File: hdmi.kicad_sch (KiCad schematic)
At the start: 44 parts, among them J13 46756-1001, Q22 NX138BKMYL, U43 NTS0102GT, U44 TPD4E02B04DQA, U45 TPD4E02B04DQA, U46 TPD4E02B04DQA

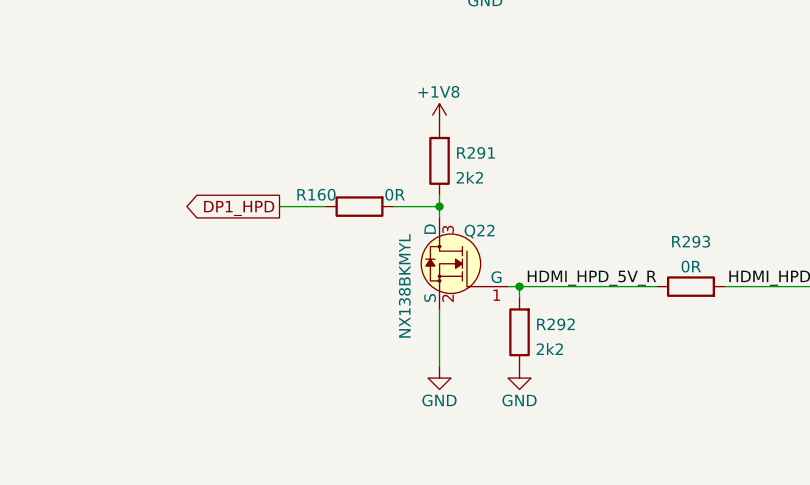
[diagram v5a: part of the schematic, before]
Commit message: Replaced NX138BKMYL with PJE138K transistor [#40527]
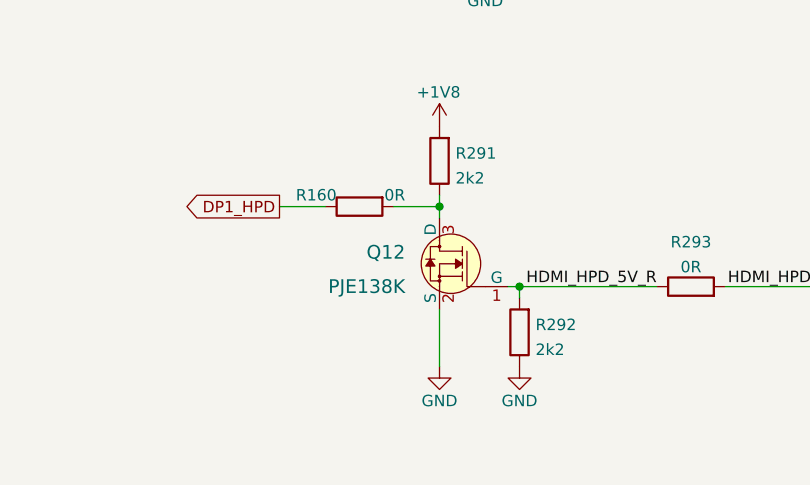
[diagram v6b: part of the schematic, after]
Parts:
- removed Q22: NX138BKMYL, jetson-orin-baseboard-footprints:DFN1006-3, symbol jetson-orin-baseboard:NX138BKMYL
- added Q12: PJE138K, antmicro-footprints:SOT-523, symbol antmicroTransistorsFETsMOSFETsSingle:PJE138K
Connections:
- net GND: now also Q12.2 (S)
- net HDMI_HPD_5V_R: now also Q12.1 (G)
- net at R160.2, R291.1: now also Q12.3 (D)
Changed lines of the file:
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@@
     (pin "2")
+  )
+  (symbol (lib_id "antmicroTransistorsFETsMOSFETsSingle:PJE138K") (at 250.19 182.88 0) (mirror y) (unit 1)
+    (in_bom yes) (on_board yes) (fields_autoplaced)
+    (property "Reference" "Q12" (id 0) (at 246.38 181.61 0)
+      (effects (font (size 1.524 1.524)) (justify left))
+    )
+    (property "Value" "PJE138K" (id 1) (at 246.38 185.42 0)
+      (effects (font (size 1.524 1.524)) (justify left))
+    )
+    (property "Footprint" "antmicro-footprints:SOT-523" (id 2) (at 245.11 177.8 0)
+      (effects (font (size 1.524 1.524)) (justify left) hide)
+    )
+    (property "Datasheet" "https://www.mouser.pl/datasheet/2/1057/PJE138K-1876698.pdf" (id 3) (at 245.11 175.26 0)
+      (effects (font (size 1.524 1.524)) (justify left) hide)
+    )
+    (property "MPN" "PJE138K_R1_00001" (id 4) (at 233.68 172.72 0)
+      (effects (font (size 1.524 1.524)) (justify left) hide)
+    )
+    (property "Manufacturer" "Panjit" (id 5) (at 245.11 172.72 0)
+      (effects (font (size 1.524 1.524)) (justify left) hide)
+    )
+    (pin "1")
+    (pin "2")
+    (pin "3")
   )
   (symbol (lib_id "jetson-orin-baseboard:C_100n_0402") (at 129.54 195.58 270) (mirror x) (unit 1)
@@
     (pin "2")
   )
-  (symbol (lib_id "jetson-orin-baseboard:NX138BKMYL") (at 250.19 182.88 0) (mirror y) (unit 1)
-    (in_bom yes) (on_board yes)
-    (property "Reference" "Q22" (id 0) (at 252.8824 179.2478 0)
-      (effects (font (size 1.27 1.27)) (justify right))
-    )
-    (property "Value" "NX138BKMYL" (id 1) (at 246.38 185.42 90))
-    (property "Footprint" "jetson-orin-baseboard-footprints:DFN1006-3" (id 2) (at 245.11 177.8 0)
-      (effects (font (size 1.524 1.524)) (justify left) hide)
-    )
-    (property "Datasheet" "https://www.mouser.pl/datasheet/2/916/NX138BKM-1919503.pdf" (id 3) (at 245.11 175.26 0)
-      (effects (font (size 1.524 1.524)) (justify left) hide)
-    )
-    (property "MPN" "NX138BKMYL" (id 4) (at 245.11 170.18 0)
-      (effects (font (size 1.524 1.524)) (justify left) hide)
-    )
-    (property "Manufacturer" "Nexperia" (id 5) (at 245.11 154.94 0)
-      (effects (font (size 1.524 1.524)) (justify left) hide)
-    )
-    (pin "1")
-    (pin "2")
-    (pin "3")
-  )
   (symbol (lib_id "jetson-orin-baseboard:C_100n_0402") (at 129.54 99.06 270) (mirror x) (unit 1)

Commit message: Replaced PCA9547 with PI4MSD5V9548AZDEX to support 1.8V I2C voltages for cameras [#40392]
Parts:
- R34, R35: footprint jetson-orin-baseboard-footprints:EXB18V -> antmicro-footprints:EXB18V; symbol jetson-orin-baseboard:4x0R_0201_array -> antmicroResistorNetworksArrays:4x0R_0201_array
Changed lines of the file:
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@@
     (pin "2")
   )
-  (symbol (lib_id "jetson-orin-baseboard:4x0R_0201_array") (at 200.66 85.09 180) (unit 1)
+  (symbol (lib_id "antmicroResistorNetworksArrays:4x0R_0201_array") (at 200.66 85.09 180) (unit 1)
     (in_bom yes) (on_board yes) (fields_autoplaced)
     (property "Reference" "R34" (id 0) (at 201.295 82.55 0))
@@
       (effects (font (size 1.524 1.524)) hide)
     )
-    (property "Footprint" "jetson-orin-baseboard-footprints:EXB18V" (id 2) (at 205.74 104.14 0)
+    (property "Footprint" "antmicro-footprints:EXB18V" (id 2) (at 205.74 104.14 0)
       (effects (font (size 1.524 1.524)) (justify left) hide)
     )
@@
     (pin "1")
   )
-  (symbol (lib_id "jetson-orin-baseboard:4x0R_0201_array") (at 201.93 115.57 0) (mirror y) (unit 1)
+  (symbol (lib_id "antmicroResistorNetworksArrays:4x0R_0201_array") (at 201.93 115.57 0) (mirror y) (unit 1)
     (in_bom yes) (on_board yes) (fields_autoplaced)
     (property "Reference" "R35" (id 0) (at 202.565 100.5672 0))
@@
       (effects (font (size 1.524 1.524)) hide)
     )
-    (property "Footprint" "jetson-orin-baseboard-footprints:EXB18V" (id 2) (at 207.01 96.52 0)
-      (effects (font (size 1.524 1.524)) (justify left) hide)
-    )
+    (property "Footprint" "antmicro-footprints:EXB18V" (id 2) (at 207.01 96.52 0)
+      (effects (font (size 1.524 1.524)) (justify left) hide)
+    )

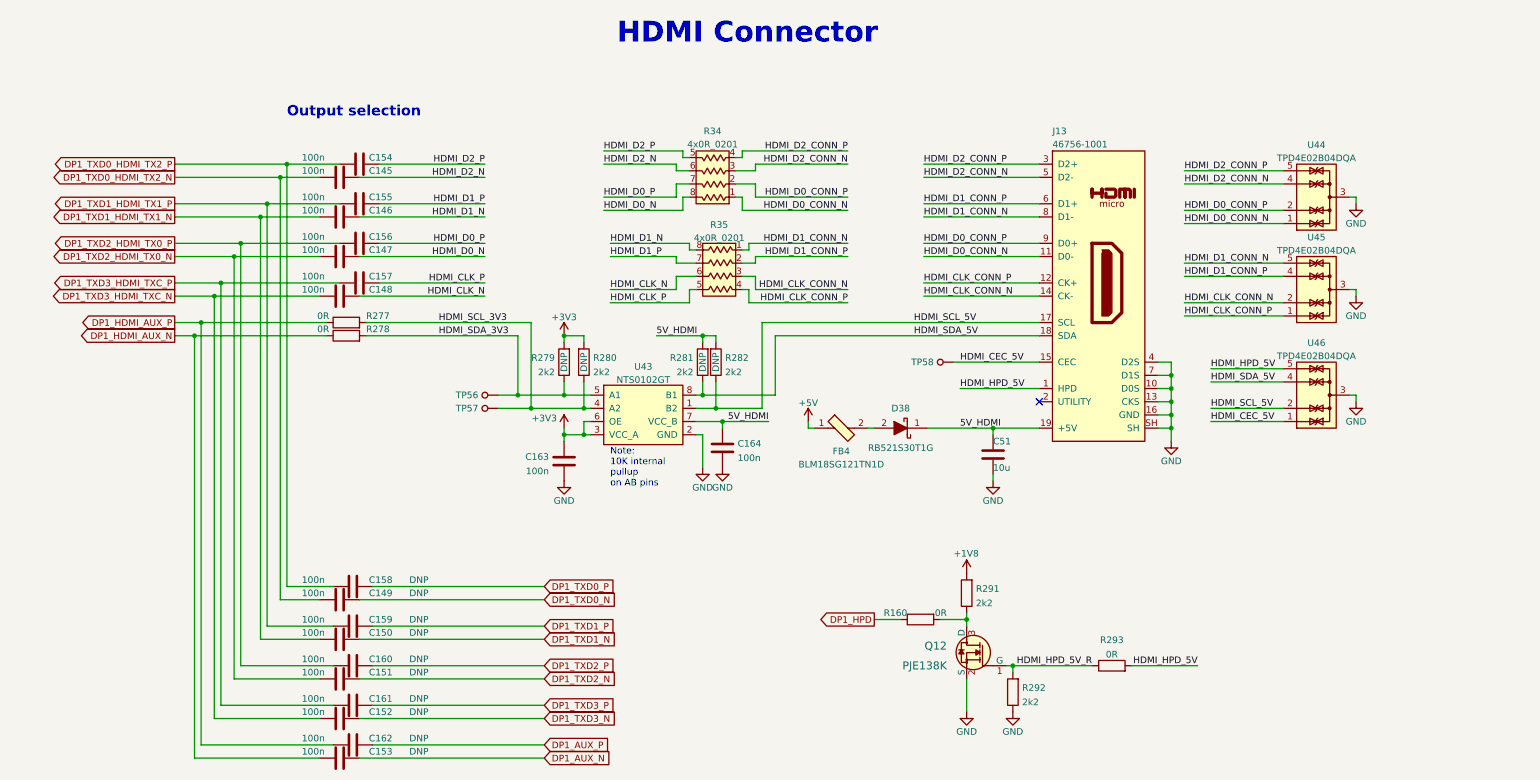
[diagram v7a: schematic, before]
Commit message: BOM reduction [#40581]
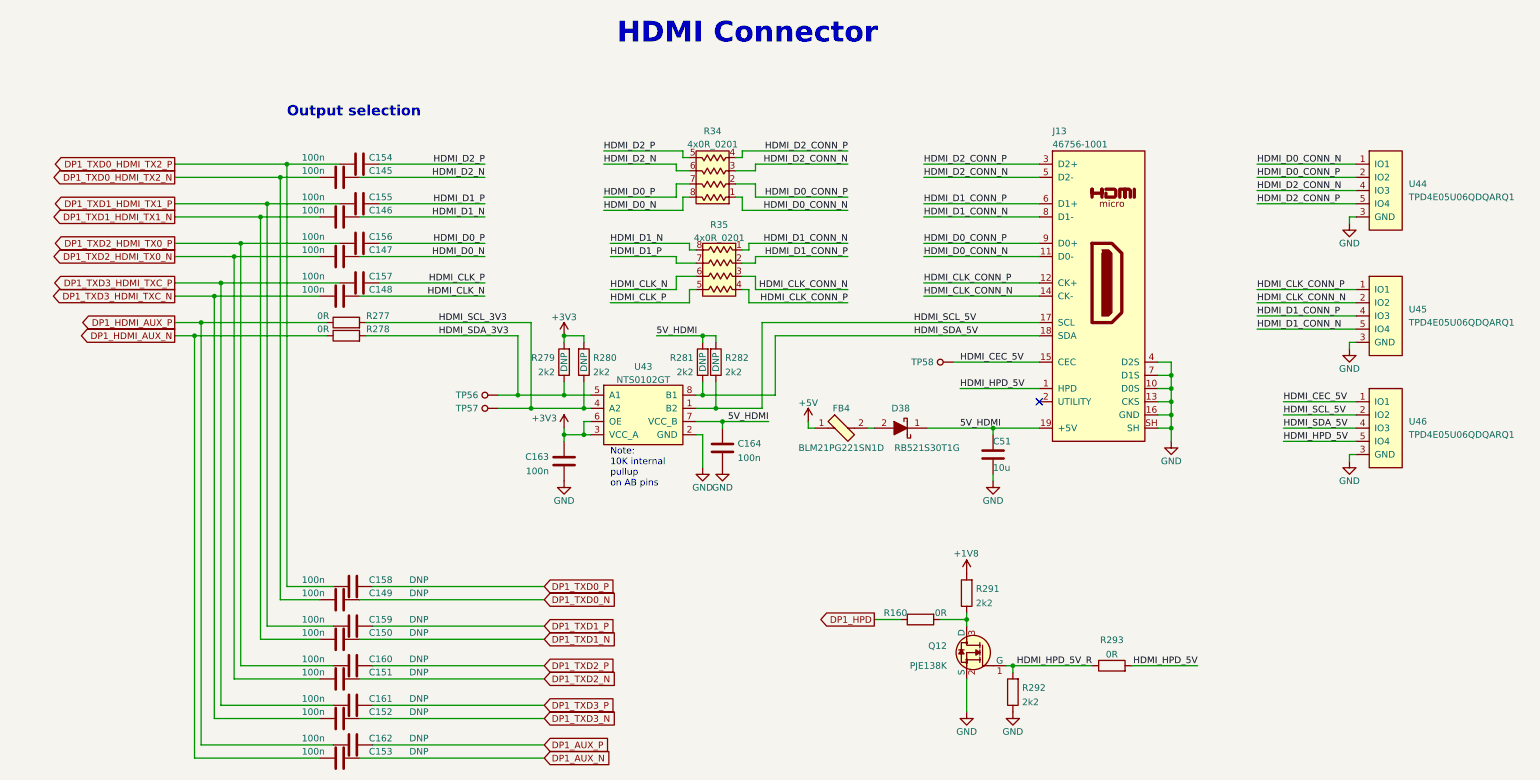
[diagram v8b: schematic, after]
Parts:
- removed FB4: BLM18SG121TN1D, jetson-orin-baseboard-footprints:0603-res, symbol jetson-orin-baseboard:BLM18SG121TN1D
- removed U44, U45, U46: TPD4E02B04DQA, jetson-orin-baseboard-footprints:USON-10_2.5x1.0mm_P0.5mm, symbol jetson-orin-baseboard:TPD4E02B04DQA
- added FB4: BLM21PG221SN1D, jetson-orin-baseboard-footprints:0805-res, symbol jetson-orin-baseboard:BLM21PG221SN1D
- added U44, U45, U46: TPD4E05U06QDQARQ1, jetson-orin-baseboard-footprints:USON-10_2.5x1.0mm_P0.5mm, symbol jetson-orin-baseboard:TPD4E05U06QDQARQ1
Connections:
- net +5V: now also FB4.1
- net GND: now also U44.3 (GND), U44.8 (GND), U45.3 (GND), U45.8 (GND), U46.3 (GND), U46.8 (GND)
- net HDMI_CEC_5V: now also U46.1 (IO1), U46.10 (IO1)
- net HDMI_CLK_CONN_N: now also U45.2 (IO2), U45.9 (IO2)
- net HDMI_CLK_CONN_P: now also U45.1 (IO1), U45.10 (IO1)
- net HDMI_D0_CONN_N: now also U44.1 (IO1), U44.10 (IO1)
- net HDMI_D0_CONN_P: now also U44.2 (IO2), U44.9 (IO2)
- net HDMI_D1_CONN_N: now also U45.5 (IO4), U45.6 (IO4)
- net HDMI_D1_CONN_P: now also U45.4 (IO3), U45.7 (IO3)
- net HDMI_D2_CONN_N: now also U44.4 (IO3), U44.7 (IO3)
- net HDMI_D2_CONN_P: now also U44.5 (IO4), U44.6 (IO4)
- net HDMI_HPD_5V: now also U46.5 (IO4), U46.6 (IO4)
- net HDMI_SCL_5V: now also U46.2 (IO2), U46.9 (IO2)
- net HDMI_SDA_5V: now also U46.4 (IO3), U46.7 (IO3)
- net at D38.2: now also FB4.2
